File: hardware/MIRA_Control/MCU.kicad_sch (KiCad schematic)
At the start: 0 parts

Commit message: Save MIRA Control and Power baseline before PCB preparation
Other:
- sheet 100_MCU_POWER_CORE renamed 100_MCU_POWER_CLOCKS_AND_DEBUG
- sheet 200_MCU_FMC_INTERFACE renamed 200_MCU_SDRAM_INTERFACE
- sheet 300_MCU_SERIAL_CONTROL renamed 300_MCU_STORAGE_AND_CONTROL
- removed sheet 400_MCU_RESERVED_GPIO
- removed sheet 500_MCU_SDRAM_64MB
- removed sheet 600_MCU_QSPI_FLASH
- removed sheet 700_MCU_MICROSD
- removed sheet 800_MCU_CLOCK_RESET_DEBUG
- sheet 100_MCU_POWER_CLOCKS_AND_DEBUG: file 100_MCU_POWER_CORE.kicad_sch -> 100_MCU_POWER_CLOCKS_AND_DEBUG.kicad_sch
- sheet 200_MCU_SDRAM_INTERFACE: file 200_MCU_FMC_INTERFACE.kicad_sch -> 200_MCU_SDRAM_INTERFACE.kicad_sch
- sheet 300_MCU_STORAGE_AND_CONTROL: file 300_MCU_SERIAL_CONTROL.kicad_sch -> 300_MCU_STORAGE_AND_CONTROL.kicad_sch

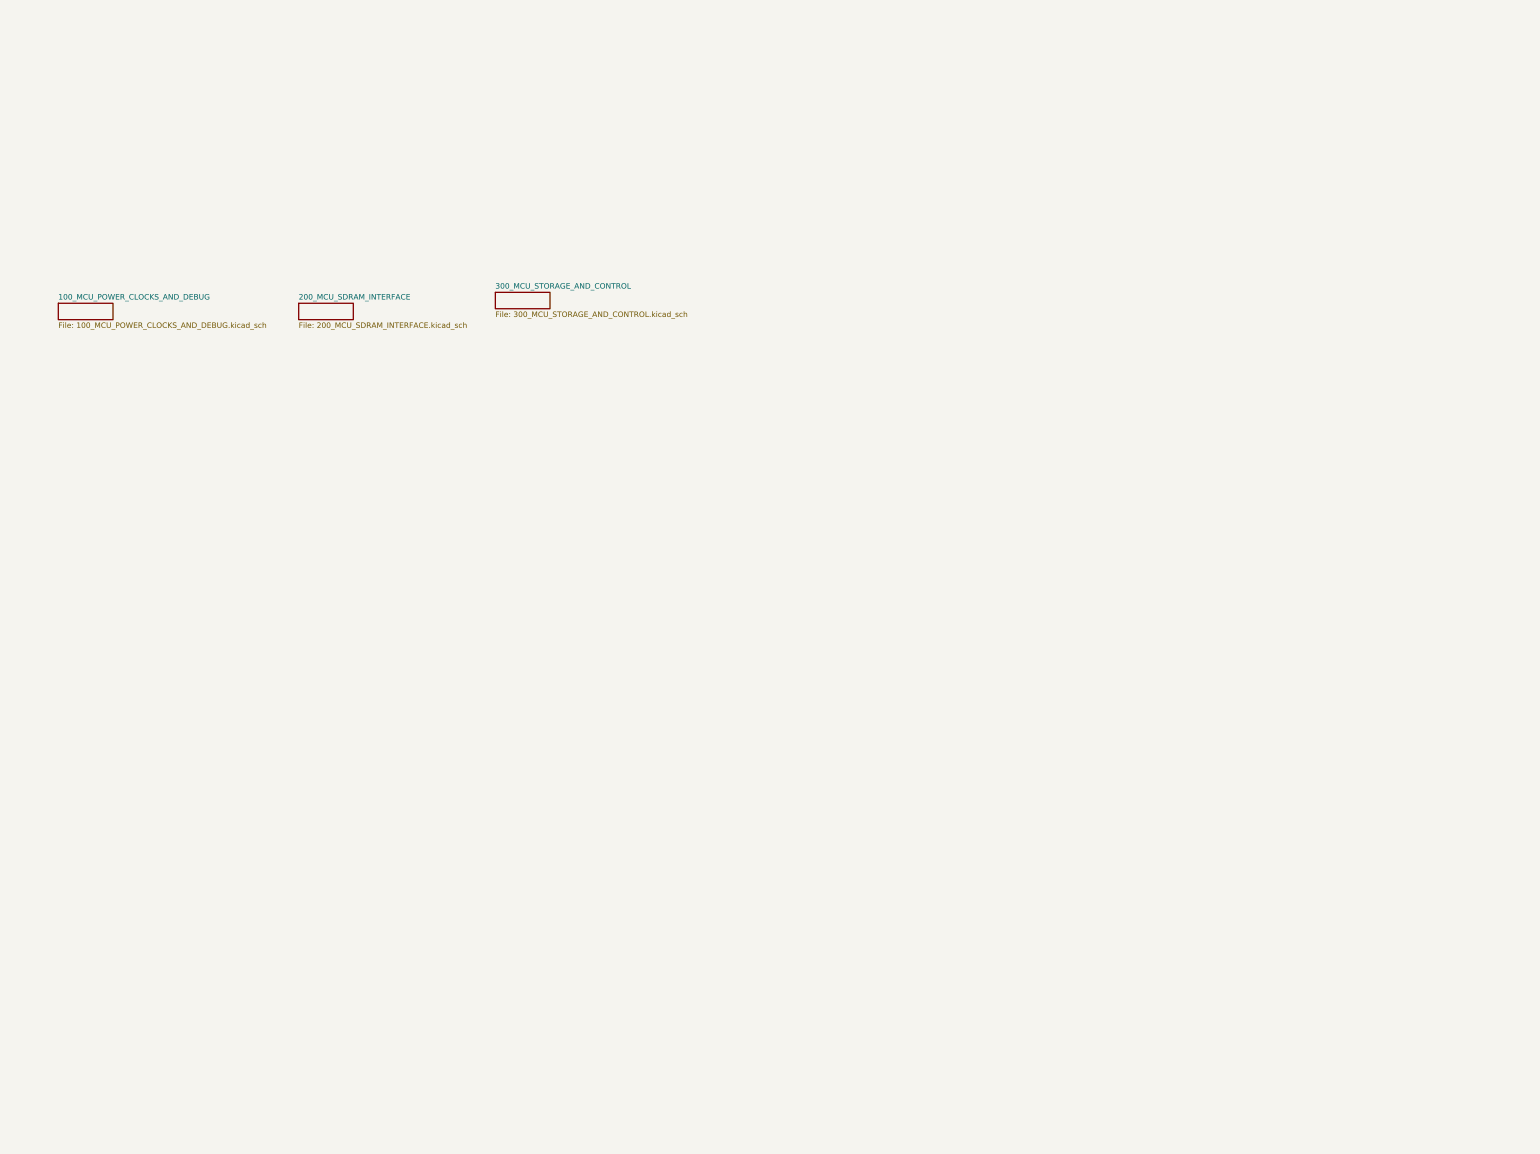
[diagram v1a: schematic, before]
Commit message: Replace Control with organized 30-page project
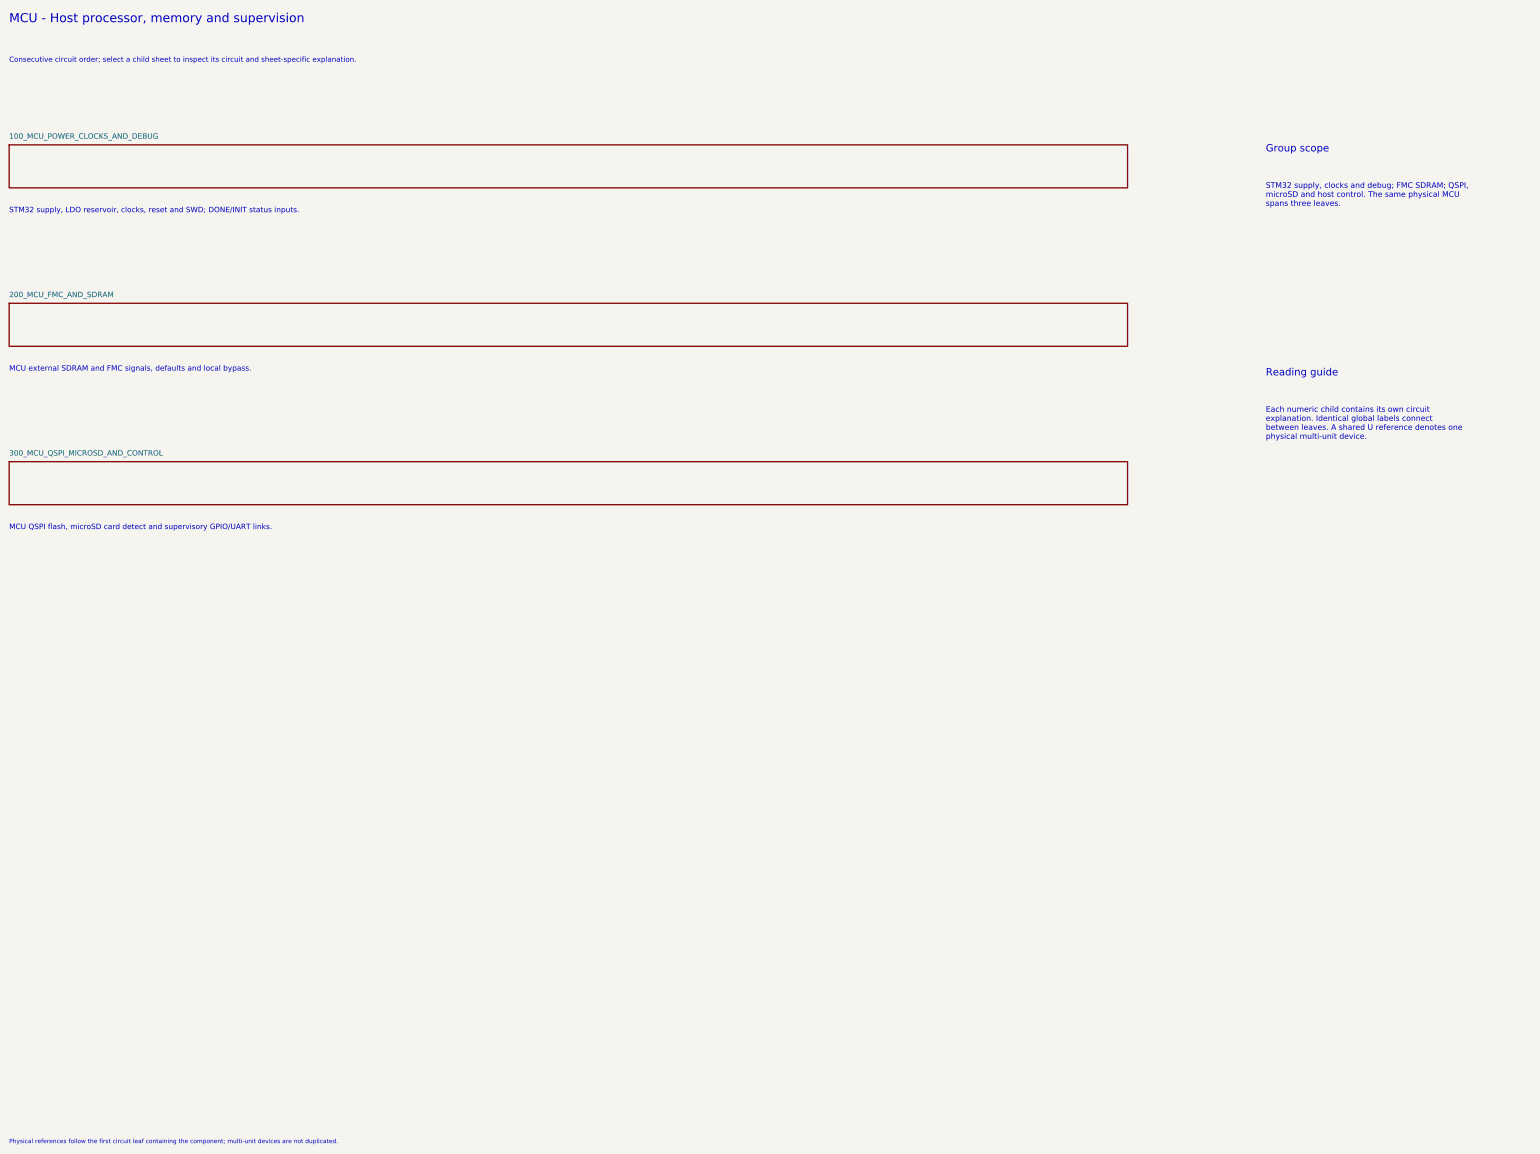
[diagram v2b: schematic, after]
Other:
- sheet 200_MCU_SDRAM_INTERFACE renamed 200_MCU_FMC_AND_SDRAM
- sheet 300_MCU_STORAGE_AND_CONTROL renamed 300_MCU_QSPI_MICROSD_AND_CONTROL
- sheet 200_MCU_FMC_AND_SDRAM: file 200_MCU_SDRAM_INTERFACE.kicad_sch -> 200_MCU_FMC_AND_SDRAM.kicad_sch
- sheet 300_MCU_QSPI_MICROSD_AND_CONTROL: file 300_MCU_STORAGE_AND_CONTROL.kicad_sch -> 300_MCU_QSPI_MICROSD_AND_CONTROL.kicad_sch
- note added: "Consecutive circuit order; select a child sheet to inspect its circuit and sheet-specific explanation."
- note added: "Each numeric child contains its own circuit explanation. Identical global labels connect between leaves. A shared U reference denotes one physical multi-unit device."
- note added: "Group scope"
- note added: "MCU - Host processor, memory and supervision"
- note added: "MCU QSPI flash, microSD card detect and supervisory GPIO/UART links."
- note added: "MCU external SDRAM and FMC signals, defaults and local bypass."
- note added: "Physical references follow the first circuit leaf containing the component; multi-unit devices are not duplicated."
- note added: "Reading guide"
- note added: "STM32 supply, LDO reservoir, clocks, reset and SWD; DONE/INIT status inputs."
- note added: "STM32 supply, clocks and debug; FMC SDRAM; QSPI, microSD and host control. The same physical MCU spans three leaves."
- company: (none) -> MIRA
- title: (none) -> Host processor, memory and supervision
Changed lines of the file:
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@@
 	(generator_version "10.0")
 	(paper "A3")
+	(title_block
+		(title "Host processor, memory and supervision")
+		(rev "B")
+		(company "MIRA")
+	)
+	(text "STM32 supply, LDO reservoir, clocks, reset and SWD; DONE/INIT status inputs."
+		(exclude_from_sim no)
+		(at 22.86 60.32 0)
+		(effects
+			(font
+				(size 1.25 1.25)
+				(color 0 70 160 1)
+			)
+			(justify left top)
+		)
+	)
+	(text "MCU QSPI flash, microSD card detect and supervisory GPIO/UART links."
+		(exclude_from_sim no)
+		(at 22.86 133.98 0)
+		(effects
+			(font
+				(size 1.25 1.25)
+				(color 0 70 160 1)
+			)
+			(justify left top)
+		)
+	)
+	(text "Group scope"
+		(exclude_from_sim no)
+		(at 315 45.72 0)
+		(effects
+			(font
+				(size 1.7 1.7)
+				(color 0 70 160 1)
+			)
+			(justify left top)
+		)
+	)
+	(text "Consecutive circuit order; select a child sheet to inspect its circuit and sheet-specific explanation."
+		(exclude_from_sim no)
+		(at 22.86 25.4 0)
+		(effects
+			(font
+				(size 1.2 1.2)
+				(color 0 70 160 1)
+			)
+			(justify left top)
+		)
+	)
+	(text "Physical references follow the first circuit leaf containing the component; multi-unit devices are not duplicated."
+		(exclude_from_sim no)
+		(at 22.86 277 0)
+		(effects
+			(font
+				(size 1 1)
+				(color 0 70 160 1)
+			)
+			(justify left top)
+		)
+	)
+	(text "Reading guide"
+		(exclude_from_sim no)
+		(at 315 97.79 0)
+		(effects
+			(font
+				(size 1.7 1.7)
+				(color 0 70 160 1)
+			)
+			(justify left top)
+		)
+	)
+	(text "MCU - Host processor, memory and supervision"
+		(exclude_from_sim no)
+		(at 22.86 15.24 0)
+		(effects
+			(font
+				(size 2.1 2.1)
+				(color 0 70 160 1)
+			)
+			(justify left top)
+		)
+	)
+	(text "STM32 supply, clocks and debug; FMC SDRAM; QSPI,\nmicroSD and host control. The same physical MCU\nspans three leaves."
+		(exclude_from_sim no)
+		(at 315 54.61 0)
+		(effects
+			(font
+				(size 1.3 1.3)
+				(color 0 70 160 1)
+			)
+			(justify left top)
+		)
+	)
+	(text "Each numeric child contains its own circuit\nexplanation. Identical global labels connect\nbetween leaves. A shared U reference denotes one\nphysical multi-unit device."
+		(exclude_from_sim no)
+		(at 315 106.68 0)
+		(effects
+			(font
+				(size 1.3 1.3)
+				(color 0 70 160 1)
+			)
+			(justify left top)
+		)
+	)
+	(text "MCU external SDRAM and FMC signals, defaults and local bypass."
+		(exclude_from_sim no)
+		(at 22.86 97.15 0)
+		(effects
+			(font
+				(size 1.25 1.25)
+				(color 0 70 160 1)
+			)
+			(justify left top)
+		)
+	)
 	(sheet
-		(at 90.17 82.55)
-		(size 12.7 3.81)
+		(at 22.86 82.55)
+		(size 260 10)
 		(exclude_from_sim no)
 		(in_bom yes)
 		(on_board yes)
 		(dnp no)
-		(fields_autoplaced yes)
 		(stroke
-			(width 0.1524)
+			(width 0.254)
 			(type solid)
 		)
@@
 			(color 0 0 0 0)
 		)
-		(property "Sheetname" "200_MCU_SDRAM_INTERFACE"
-			(at 90.17 81.8384 0)
-			(show_name no)
-			(do_not_autoplace no)
-			(effects
-				(font
-					(size 1.27 1.27)
+		(property "Sheetname" "200_MCU_FMC_AND_SDRAM"
+			(at 22.86 81.28 0)
+			(show_name no)
+			(do_not_autoplace no)
+			(effects
+				(font
+					(size 1.25 1.25)
 				)
 				(justify left bottom)
 			)
 		)
-		(property "Sheetfile" "200_MCU_SDRAM_INTERFACE.kicad_sch"
-			(at 90.17 86.9446 0)
-			(show_name no)
-			(do_not_autoplace no)
-			(effects
-				(font
-					(size 1.27 1.27)
+		(property "Sheetfile" "200_MCU_FMC_AND_SDRAM.kicad_sch"
+			(at 22.86 93.82 0)
+			(hide yes)
+			(show_name no)
+			(do_not_autoplace no)
+			(effects
+				(font
+					(size 1 1)
 				)
 				(justify left top)
@@
 	)
 	(sheet
-		(at 34.29 82.55)
-		(size 12.7 3.81)
+		(at 22.86 45.72)
+		(size 260 10)
 		(exclude_from_sim no)
 		(in_bom yes)
 		(on_board yes)
 		(dnp no)
-		(fields_autoplaced yes)
 		(stroke
-			(width 0.1524)
+			(width 0.254)
 			(type solid)
 		)
@@
 		)
 		(property "Sheetname" "100_MCU_POWER_CLOCKS_AND_DEBUG"
-			(at 34.29 81.8384 0)
-			(show_name no)
-			(do_not_autoplace no)
-			(effects
-				(font
-					(size 1.27 1.27)
+			(at 22.86 44.45 0)
+			(show_name no)
+			(do_not_autoplace no)
+			(effects
+				(font
+					(size 1.25 1.25)
 				)
 				(justify left bottom)
@@
 		)
 		(property "Sheetfile" "100_MCU_POWER_CLOCKS_AND_DEBUG.kicad_sch"
-			(at 34.29 86.9446 0)
-			(show_name no)
-			(do_not_autoplace no)
-			(effects
-				(font
-					(size 1.27 1.27)
+			(at 22.86 56.99 0)
+			(hide yes)
+			(show_name no)
+			(do_not_autoplace no)
+			(effects
+				(font
+					(size 1 1)
 				)
 				(justify left top)
@@
 	)
 	(sheet
-		(at 135.89 80.01)
-		(size 12.7 3.81)
+		(at 22.86 119.38)
+		(size 260 10)
 		(exclude_from_sim no)
 		(in_bom yes)
 		(on_board yes)
 		(dnp no)
-		(fields_autoplaced yes)
 		(stroke
-			(width 0.1524)
+			(width 0.254)
 			(type solid)
 		)
@@
 			(color 0 0 0 0)
 		)
-		(property "Sheetname" "300_MCU_STORAGE_AND_CONTROL"
-			(at 135.89 79.2984 0)
-			(show_name no)
-			(do_not_autoplace no)
-			(effects
-				(font
-					(size 1.27 1.27)
+		(property "Sheetname" "300_MCU_QSPI_MICROSD_AND_CONTROL"
+			(at 22.86 118.11 0)
+			(show_name no)
+			(do_not_autoplace no)
+			(effects
+				(font
+					(size 1.25 1.25)
 				)
 				(justify left bottom)
 			)
 		)
-		(property "Sheetfile" "300_MCU_STORAGE_AND_CONTROL.kicad_sch"
-			(at 135.89 84.4046 0)
-			(show_name no)
-			(do_not_autoplace no)
-			(effects
-				(font
-					(size 1.27 1.27)
+		(property "Sheetfile" "300_MCU_QSPI_MICROSD_AND_CONTROL.kicad_sch"
+			(at 22.86 130.65 0)
+			(hide yes)
+			(show_name no)
+			(do_not_autoplace no)
+			(effects
+				(font
+					(size 1 1)
 				)
 				(justify left top)
